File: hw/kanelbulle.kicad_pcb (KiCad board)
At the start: 2 copper layers, 48.8 x 48.8 mm, 0 parts

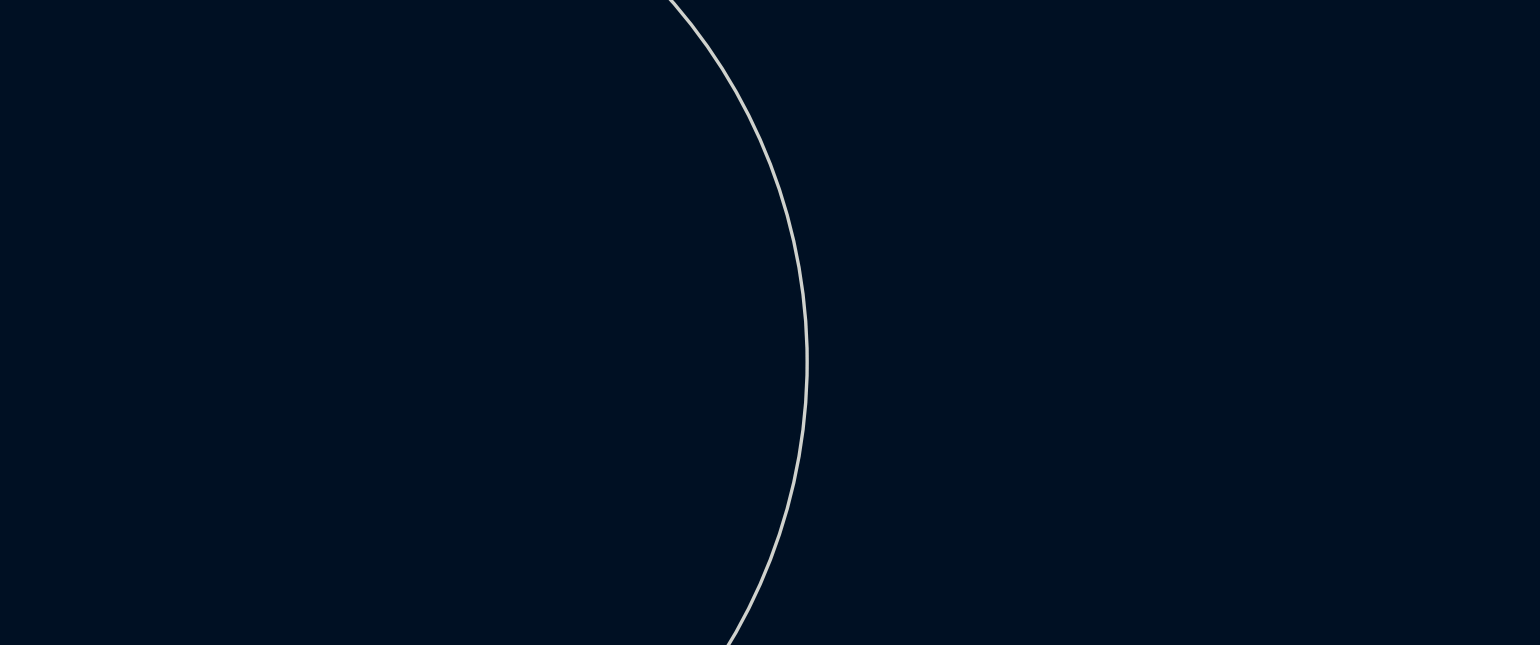
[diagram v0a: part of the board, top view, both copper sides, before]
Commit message: added micro controller to schematic
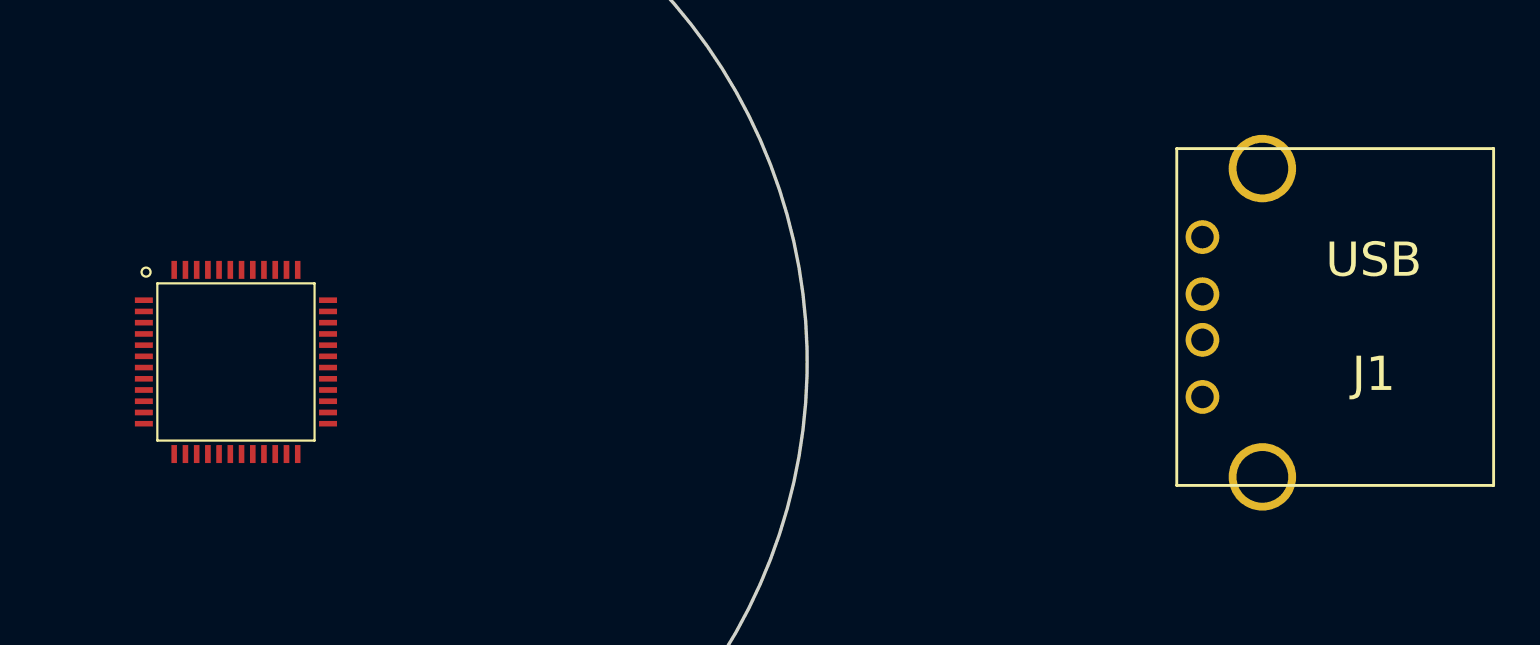
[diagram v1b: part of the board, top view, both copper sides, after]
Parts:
- added J1: USB, USB_A, F.Cu at (209.0, 109.0)
- added U1: LPC1114/302, LQFP48, F.Cu at (166.0, 111.0)
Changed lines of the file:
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@@
     (links 0)
     (no_connects 0)
-    (area 0 0 0 0)
+    (area 125.541668 76.925001 222.271501 136.000001)
     (thickness 1.6)
     (drawings 5)
     (tracks 0)
     (zones 0)
-    (modules 0)
+    (modules 2)
     (nets 1)
   )
@@
     (add_net "")
   )
+  (module USB_A (layer F.Cu)
+    (at 209 109)
+    (fp_text reference J1 (at 7.62 2.54) (layer F.SilkS)
+      (effects (font (size 1.524 1.524) (thickness 0.3048)))
+    )
+    (fp_text value USB (at 7.62 -2.54) (layer F.SilkS)
+      (effects (font (size 1.524 1.524) (thickness 0.3048)))
+    )
+    (fp_line (start -1.143 -7.493) (end 12.954 -7.493) (layer F.SilkS) (width 0.127))
+    (fp_line (start 12.954 7.493) (end -1.143 7.493) (layer F.SilkS) (width 0.127))
+    (fp_line (start -1.143 -7.493) (end -1.143 7.493) (layer F.SilkS) (width 0.127))
+    (fp_line (start 12.954 -7.493) (end 12.954 7.493) (layer F.SilkS) (width 0.127))
+    (pad 4 thru_hole circle (at 0 -3.556) (size 1.50114 1.50114) (drill 1.00076)
+      (layers *.Cu *.Mask F.SilkS)
+    )
+    (pad 3 thru_hole circle (at 0 -1.016) (size 1.50114 1.50114) (drill 1.00076)
+      (layers *.Cu *.Mask F.SilkS)
+    )
+    (pad 2 thru_hole circle (at 0 1.016) (size 1.50114 1.50114) (drill 1.00076)
+      (layers *.Cu *.Mask F.SilkS)
+    )
+    (pad 1 thru_hole circle (at 0 3.556) (size 1.50114 1.50114) (drill 1.00076)
+      (layers *.Cu *.Mask F.SilkS)
+    )
+    (pad 5 thru_hole circle (at 2.667 -6.604) (size 2.99974 2.99974) (drill 2.30124)
+      (layers *.Cu *.Mask F.SilkS)
+    )
+    (pad 6 thru_hole circle (at 2.667 7.112) (size 2.99974 2.99974) (drill 2.30124)
+      (layers *.Cu *.Mask F.SilkS)
+    )
+    (model connectors/usb_a_through_hole.wrl
+      (at (xyz 0 0 0))
+      (scale (xyz 1 1 1))
+      (rotate (xyz 0 0 0))
+    )
+  )
+  (module LQFP48 (layer F.Cu)
+    (at 166 111)
+    (attr smd)
+    (fp_text reference U1 (at 0 -0.381) (layer Cmts.User)
+      (effects (font (size 0.508 0.508) (thickness 0.1016)))
+    )
+    (fp_text value LPC1114/302 (at 0 0.381) (layer Cmts.User) hide
+      (effects (font (size 0.508 0.508) (thickness 0.1016)))
+    )
+    (fp_circle (center -3.99796 -3.99796) (end -3.99796 -4.19862) (layer F.SilkS) (width 0.09906))
+    (fp_line (start -3.49758 -3.49758) (end -3.49758 3.49758) (layer F.SilkS) (width 0.09906))
+    (fp_line (start -3.49758 3.49758) (end 3.49758 3.49758) (layer F.SilkS) (width 0.09906))
+    (fp_line (start 3.49758 3.49758) (end 3.49758 -3.49758) (layer F.SilkS) (width 0.09906))
+    (fp_line (start 3.49758 -3.49758) (end -3.49758 -3.49758) (layer F.SilkS) (width 0.09906))
+    (pad 12 smd rect (at -4.09702 2.74828) (size 0.8001 0.24892)
+      (layers F.Cu F.Paste F.Mask)
+    )
+    (pad 11 smd rect (at -4.09702 2.2479) (size 0.8001 0.25146)
+      (layers F.Cu F.Paste F.Mask)
+    )
+    (pad 10 smd rect (at -4.09702 1.74752) (size 0.8001 0.25146)
+      (layers F.Cu F.Paste F.Mask)
+    )
+    (pad 9 smd rect (at -4.09702 1.24714) (size 0.8001 0.25146)
+      (layers F.Cu F.Paste F.Mask)
+    )
+    (pad 8 smd rect (at -4.09702 0.7493) (size 0.8001 0.24892)
+      (layers F.Cu F.Paste F.Mask)
+    )
+    (pad 7 smd rect (at -4.09702 0.24892) (size 0.8001 0.24892)
+      (layers F.Cu F.Paste F.Mask)
+    )
+    (pad 6 smd rect (at -4.09702 -0.24892) (size 0.8001 0.24892)
+      (layers F.Cu F.Paste F.Mask)
+    )
+    (pad 5 smd rect (at -4.09702 -0.7493) (size 0.8001 0.24892)
+      (layers F.Cu F.Paste F.Mask)
+    )
+    (pad 4 smd rect (at -4.09702 -1.24714) (size 0.8001 0.25146)
+      (layers F.Cu F.Paste F.Mask)
+    )
+    (pad 3 smd rect (at -4.09702 -1.74752) (size 0.8001 0.25146)
+      (layers F.Cu F.Paste F.Mask)
+    )
+    (pad 2 smd rect (at -4.09702 -2.2479) (size 0.8001 0.25146)
+      (layers F.Cu F.Paste F.Mask)
+    )
+    (pad 1 smd rect (at -4.09702 -2.74828) (size 0.8001 0.24892)
+      (layers F.Cu F.Paste F.Mask)
+    )
+    (pad 48 smd rect (at -2.74828 -4.09702) (size 0.24892 0.8001)
+      (layers F.Cu F.Paste F.Mask)
+    )
+    (pad 47 smd rect (at -2.2479 -4.09702) (size 0.25146 0.8001)
+      (layers F.Cu F.Paste F.Mask)
+    )
+    (pad 46 smd rect (at -1.74752 -4.09702) (size 0.25146 0.8001)
+      (layers F.Cu F.Paste F.Mask)
+    )
+    (pad 45 smd rect (at -1.24714 -4.09702) (size 0.25146 0.8001)
+      (layers F.Cu F.Paste F.Mask)
+    )
+    (pad 44 smd rect (at -0.7493 -4.09702) (size 0.24892 0.8001)
+      (layers F.Cu F.Paste F.Mask)
+    )
+    (pad 43 smd rect (at -0.24892 -4.09702) (size 0.24892 0.8001)
+      (layers F.Cu F.Paste F.Mask)
+    )
+    (pad 42 smd rect (at 0.24892 -4.09702) (size 0.24892 0.8001)
+      (layers F.Cu F.Paste F.Mask)
+    )
+    (pad 41 smd rect (at 0.7493 -4.09702) (size 0.24892 0.8001)
+      (layers F.Cu F.Paste F.Mask)
+    )
+    (pad 40 smd rect (at 1.24714 -4.09702) (size 0.25146 0.8001)
+      (layers F.Cu F.Paste F.Mask)
+    )
+    (pad 39 smd rect (at 1.74752 -4.09702) (size 0.25146 0.8001)
+      (layers F.Cu F.Paste F.Mask)
+    )
+    (pad 38 smd rect (at 2.2479 -4.09702) (size 0.25146 0.8001)
+      (layers F.Cu F.Paste F.Mask)
+    )
+    (pad 37 smd rect (at 2.74828 -4.09702) (size 0.24892 0.8001)
+      (layers F.Cu F.Paste F.Mask)
+    )
+    (pad 25 smd rect (at 4.09702 2.74828) (size 0.8001 0.24892)
+      (layers F.Cu F.Paste F.Mask)
+    )
+    (pad 26 smd rect (at 4.09702 2.2479) (size 0.8001 0.25146)
+      (layers F.Cu F.Paste F.Mask)
+    )
+    (pad 27 smd rect (at 4.09702 1.74752) (size 0.8001 0.25146)
+      (layers F.Cu F.Paste F.Mask)
+    )
+    (pad 28 smd rect (at 4.09702 1.24714) (size 0.8001 0.25146)
+      (layers F.Cu F.Paste F.Mask)
+    )
+    (pad 29 smd rect (at 4.09702 0.7493) (size 0.8001 0.24892)
+      (layers F.Cu F.Paste F.Mask)
+    )
+    (pad 30 smd rect (at 4.09702 0.24892) (size 0.8001 0.24892)
+      (layers F.Cu F.Paste F.Mask)
+    )
+    (pad 31 smd rect (at 4.09702 -0.24892) (size 0.8001 0.24892)
+      (layers F.Cu F.Paste F.Mask)
+    )
+    (pad 32 smd rect (at 4.09702 -0.7493) (size 0.8001 0.24892)
+      (layers F.Cu F.Paste F.Mask)
+    )
+    (pad 33 smd rect (at 4.09702 -1.24714) (size 0.8001 0.25146)
+      (layers F.Cu F.Paste F.Mask)
+    )
+    (pad 34 smd rect (at 4.09702 -1.74752) (size 0.8001 0.25146)
+      (layers F.Cu F.Paste F.Mask)
+    )
+    (pad 35 smd rect (at 4.09702 -2.2479) (size 0.8001 0.25146)
+      (layers F.Cu F.Paste F.Mask)
+    )
+    (pad 36 smd rect (at 4.09702 -2.74828) (size 0.8001 0.24892)
+      (layers F.Cu F.Paste F.Mask)
+    )
+    (pad 13 smd rect (at -2.74828 4.09702) (size 0.24892 0.8001)
+      (layers F.Cu F.Paste F.Mask)
+    )
+    (pad 14 smd rect (at -2.2479 4.09702) (size 0.25146 0.8001)
+      (layers F.Cu F.Paste F.Mask)
+    )
+    (pad 15 smd rect (at -1.74752 4.09702) (size 0.25146 0.8001)
+      (layers F.Cu F.Paste F.Mask)
+    )
+    (pad 16 smd rect (at -1.24714 4.09702) (size 0.25146 0.8001)
+      (layers F.Cu F.Paste F.Mask)
+    )
+    (pad 17 smd rect (at -0.7493 4.09702) (size 0.24892 0.8001)
+      (layers F.Cu F.Paste F.Mask)
+    )
+    (pad 18 smd rect (at -0.24892 4.09702) (size 0.24892 0.8001)
+      (layers F.Cu F.Paste F.Mask)
+    )
+    (pad 19 smd rect (at 0.24892 4.09702) (size 0.24892 0.8001)
+      (layers F.Cu F.Paste F.Mask)
+    )
+    (pad 20 smd rect (at 0.7493 4.09702) (size 0.24892 0.8001)
+      (layers F.Cu F.Paste F.Mask)
+    )
+    (pad 21 smd rect (at 1.24714 4.09702) (size 0.25146 0.8001)
+      (layers F.Cu F.Paste F.Mask)
+    )
+    (pad 22 smd rect (at 1.74752 4.09702) (size 0.25146 0.8001)
+      (layers F.Cu F.Paste F.Mask)
+    )
+    (pad 23 smd rect (at 2.2479 4.09702) (size 0.25146 0.8001)
+      (layers F.Cu F.Paste F.Mask)
+    )
+    (pad 24 smd rect (at 2.74828 4.09702) (size 0.24892 0.8001)
+      (layers F.Cu F.Paste F.Mask)
+    )
+  )
   (gr_circle (center 167 111) (end 147 97) (layer Edge.Cuts) (width 0.15))

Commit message: leds, leds everywhere
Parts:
- added D1: LED_RGB, PLCC4, F.Cu at (153.7, 127.0)
- added D10: LED_RGB, PLCC4, F.Cu at (182.4, 96.8)
- added D11: LED_RGB, PLCC4, F.Cu at (178.3, 92.7)
- added D12: LED_RGB, PLCC4, F.Cu at (173.0, 91.2)
- added D13: LED_RGB, PLCC4, F.Cu at (167.9, 89.7)
- added D14: LED_RGB, PLCC4, F.Cu at (188.5, 106.7)
- added D15: LED_RGB, PLCC4, F.Cu at (149.4, 121.7)
- added D16: LED_RGB, PLCC4, F.Cu at (146.1, 116.3)
- added D17: LED_RGB, PLCC4, F.Cu at (147.3, 103.4)
- added D18: LED_RGB, PLCC4, F.Cu at (144.8, 110.0)
- added D19: LED_RGB, PLCC4, F.Cu at (151.4, 97.3)
- added D2: LED_RGB, PLCC4, F.Cu at (189.2, 112.5)
- added D20: LED_RGB, PLCC4, F.Cu at (159.5, 90.9)
- added D21: LED_RGB, PLCC4, F.Cu at (168.4, 95.8)
- added D22: LED_RGB, PLCC4, F.Cu at (158.8, 98.0)
- added D23: LED_RGB, PLCC4, F.Cu at (163.3, 96.0)
- added D24: LED_RGB, PLCC4, F.Cu at (152.9, 106.7)
- added D25: LED_RGB, PLCC4, F.Cu at (155.7, 102.1)
- added D26: LED_RGB, PLCC4, F.Cu at (174.2, 98.0)
- added D27: LED_RGB, PLCC4, F.Cu at (178.3, 99.6)
- added D28: LED_RGB, PLCC4, F.Cu at (181.4, 104.1)
- added D29: LED_RGB, PLCC4, F.Cu at (184.4, 111.3)
- added D3: LED_RGB, PLCC4, F.Cu at (184.7, 122.7)
- added D30: LED_RGB, PLCC4, F.Cu at (182.1, 118.1)
- added D31: LED_RGB, PLCC4, F.Cu at (178.1, 122.7)
- added D32: LED_RGB, PLCC4, F.Cu at (171.4, 126.0)
- added D33: LED_RGB, PLCC4, F.Cu at (164.1, 126.0)
- added D34: LED_RGB, PLCC4, F.Cu at (159.0, 123.7)
- added D35: LED_RGB, PLCC4, F.Cu at (154.7, 118.4)
- added D36: LED_RGB, PLCC4, F.Cu at (151.1, 112.3)
- added D37: LED_RGB, PLCC4, F.Cu at (167.1, 101.3)
- added D38: LED_RGB, PLCC4, F.Cu at (173.2, 103.9)
- added D39: LED_RGB, PLCC4, F.Cu at (178.3, 108.2)
- added D4: LED_RGB, PLCC4, F.Cu at (180.6, 127.8)
- added D40: LED_RGB, PLCC4, F.Cu at (178.1, 114.3)
- added D41: LED_RGB, PLCC4, F.Cu at (173.7, 119.6)
- added D42: LED_RGB, PLCC4, F.Cu at (167.1, 121.2)
- added D43: LED_RGB, PLCC4, F.Cu at (161.0, 116.6)
- added D44: LED_RGB, PLCC4, F.Cu at (157.0, 111.3)
- added D45: LED_RGB, PLCC4, F.Cu at (161.0, 103.1)
- added D46: LED_RGB, PLCC4, F.Cu at (163.3, 112.3)
- added D47: LED_RGB, PLCC4, F.Cu at (169.2, 116.6)
- added D48: LED_RGB, PLCC4, F.Cu at (174.2, 114.3)
- added D49: LED_RGB, PLCC4, F.Cu at (171.2, 108.2)
- added D5: LED_RGB, PLCC4, F.Cu at (175.3, 130.0)
- added D50: LED_RGB, PLCC4, F.Cu at (163.8, 106.9)
- added D51: LED_RGB, PLCC4, F.Cu at (167.4, 110.5)
- added D6: LED_RGB, PLCC4, F.Cu at (167.6, 132.1)
- added D7: LED_RGB, PLCC4, F.Cu at (188.0, 117.6)
- added D8: LED_RGB, PLCC4, F.Cu at (160.8, 130.3)
- added D9: LED_RGB, PLCC4, F.Cu at (186.4, 100.8)
- U1: moved to B.Cu
- moved J1 14.0 mm to (209.3, 95.0)
- moved U1 13.6 mm to (176.3, 102.1)

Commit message: added led driver chip
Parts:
- added U2: PCA9685, tssop-28, B.Cu at (176.3, 115.1)
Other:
- net class Default: clearance 0.254 -> 0.2032
- rule trace_clearance: 0.254 -> 0.2032
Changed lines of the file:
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@@
     (links 0)
     (no_connects 0)
-    (area 125.541668 55.173637 222.567501 136.000001)
+    (area 142.511888 86.511888 191.488112 135.488112)
     (thickness 1.6)
     (drawings 5)
     (tracks 0)
     (zones 0)
-    (modules 53)
+    (modules 54)
     (nets 1)
   )
@@
   (setup
     (last_trace_width 0.254)
-    (trace_clearance 0.254)
+    (trace_clearance 0.2032)
     (zone_clearance 0.508)
     (zone_45_only no)
@@
   (net 0 "")
   (net_class Default "This is the default net class."
-    (clearance 0.254)
+    (clearance 0.2032)
     (trace_width 0.254)
     (via_dia 0.889)
@@
     )
   )
+  (module tssop-28 (layer B.Cu)
+    (at 176.276 115.062)
+    (descr TSSOP-28)
+    (fp_text reference U2 (at 0 -0.508) (layer B.SilkS)
+      (effects (font (size 0.50038 0.50038) (thickness 0.09906)) (justify mirror))
+    )
+    (fp_text value PCA9685 (at 0 1.143) (layer B.SilkS)
+      (effects (font (size 0.50038 0.50038) (thickness 0.09906)) (justify mirror))
+    )
+    (fp_line (start 4.953 2.286) (end -4.953 2.286) (layer B.SilkS) (width 0.127))
+    (fp_line (start -4.953 2.286) (end -4.953 -2.286) (layer B.SilkS) (width 0.127))
+    (fp_line (start -4.953 -2.286) (end 4.953 -2.286) (layer B.SilkS) (width 0.127))
+    (fp_line (start 4.953 -2.286) (end 4.953 2.286) (layer B.SilkS) (width 0.127))
+    (fp_circle (center -4.064 -1.524) (end -4.191 -1.778) (layer B.SilkS) (width 0.127))
+    (pad 7 smd rect (at -0.32512 -2.79908) (size 0.4191 1.47066)
+      (layers B.Cu B.Paste B.Mask)
+    )
+    (pad 8 smd rect (at 0.32512 -2.79908) (size 0.4191 1.47066)
+      (layers B.Cu B.Paste B.Mask)
+    )
+    (pad 9 smd rect (at 0.97536 -2.79908) (size 0.4191 1.47066)
+      (layers B.Cu B.Paste B.Mask)
+    )
+    (pad 10 smd rect (at 1.6256 -2.79908) (size 0.4191 1.47066)
+      (layers B.Cu B.Paste B.Mask)
+    )
+    (pad 25 smd rect (at -2.26568 2.794) (size 0.4191 1.47066)
+      (layers B.Cu B.Paste B.Mask)
+    )
+    (pad 4 smd rect (at -2.27584 -2.79908) (size 0.4191 1.47066)
+      (layers B.Cu B.Paste B.Mask)
+    )
+    (pad 5 smd rect (at -1.6256 -2.79908) (size 0.4191 1.47066)
+      (layers B.Cu B.Paste B.Mask)
+    )
+    (pad 6 smd rect (at -0.97536 -2.79908) (size 0.4191 1.47066)
+      (layers B.Cu B.Paste B.Mask)
+    )
+    (pad 18 smd rect (at 2.27584 2.79908) (size 0.4191 1.47066)
+      (layers B.Cu B.Paste B.Mask)
+    )
+    (pad 19 smd rect (at 1.6256 2.79908) (size 0.4191 1.47066)
+      (layers B.Cu B.Paste B.Mask)
+    )
+    (pad 20 smd rect (at 0.97536 2.79908) (size 0.4191 1.47066)
+      (layers B.Cu B.Paste B.Mask)
+    )
+    (pad 21 smd rect (at 0.32512 2.79908) (size 0.4191 1.47066)
+      (layers B.Cu B.Paste B.Mask)
+    )
+    (pad 22 smd rect (at -0.32512 2.79908) (size 0.4191 1.47066)
+      (layers B.Cu B.Paste B.Mask)
+    )
+    (pad 23 smd rect (at -0.97536 2.79908) (size 0.4191 1.47066)
+      (layers B.Cu B.Paste B.Mask)
+    )
+    (pad 11 smd rect (at 2.27584 -2.79908) (size 0.4191 1.47066)
+      (layers B.Cu B.Paste B.Mask)
+    )
+    (pad 24 smd rect (at -1.6256 2.794) (size 0.4191 1.47066)
+      (layers B.Cu B.Paste B.Mask)
+    )
+    (pad 3 smd rect (at -2.92608 -2.79908) (size 0.4191 1.47066)
+      (layers B.Cu B.Paste B.Mask)
+    )
+    (pad 12 smd rect (at 2.92608 -2.79908) (size 0.4191 1.47066)
+      (layers B.Cu B.Paste B.Mask)
+    )
+    (pad 17 smd rect (at 2.92608 2.79908) (size 0.4191 1.47066)
+      (layers B.Cu B.Paste B.Mask)
+    )
+    (pad 26 smd rect (at -2.92608 2.79908) (size 0.4191 1.47066)
+      (layers B.Cu B.Paste B.Mask)
+    )
+    (pad 2 smd rect (at -3.57378 -2.79908) (size 0.4191 1.47066)
+      (layers B.Cu B.Paste B.Mask)
+    )
+    (pad 13 smd rect (at 3.57378 -2.79908) (size 0.4191 1.47066)
+      (layers B.Cu B.Paste B.Mask)
+    )
+    (pad 16 smd rect (at 3.57378 2.79908) (size 0.4191 1.47066)
+      (layers B.Cu B.Paste B.Mask)
+    )
+    (pad 27 smd rect (at -3.57378 2.79908) (size 0.4191 1.47066)
+      (layers B.Cu B.Paste B.Mask)
+    )
+    (pad 1 smd rect (at -4.22402 -2.79908) (size 0.4191 1.47066)
+      (layers B.Cu B.Paste B.Mask)
+    )
+    (pad 14 smd rect (at 4.22402 -2.79908) (size 0.4191 1.47066)
+      (layers B.Cu B.Paste B.Mask)
+    )
+    (pad 15 smd rect (at 4.22402 2.79908) (size 0.4191 1.47066)
+      (layers B.Cu B.Paste B.Mask)
+    )
+    (pad 28 smd rect (at -4.22402 2.79908) (size 0.4191 1.47066)
+      (layers B.Cu B.Paste B.Mask)
+    )
+    (model smd/smd_dil/tssop-28.wrl
+      (at (xyz 0 0 0))
+      (scale (xyz 1 1 1))
+      (rotate (xyz 0 0 0))
+    )
+  )

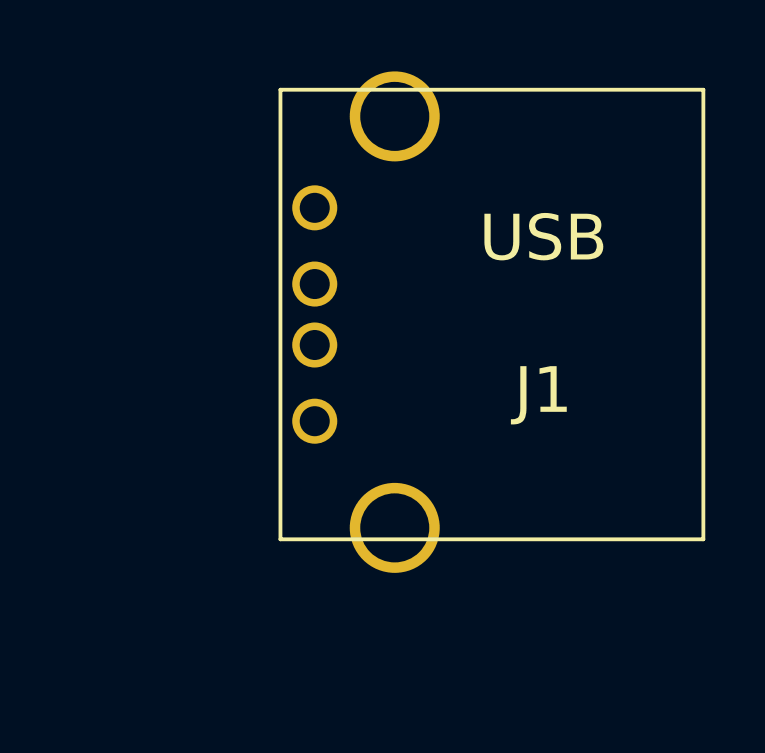
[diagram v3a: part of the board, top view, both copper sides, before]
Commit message: added led 3d model
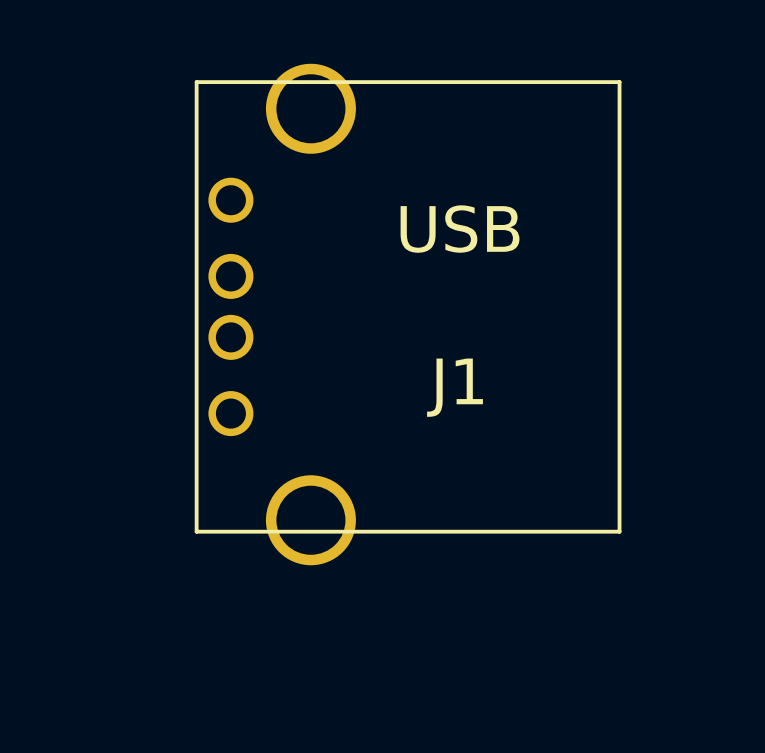
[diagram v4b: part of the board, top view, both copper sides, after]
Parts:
- moved J1 2.81 mm to (206.5, 94.7)
